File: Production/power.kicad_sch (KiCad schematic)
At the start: 4 parts, among them U204 TPS62177DQCR

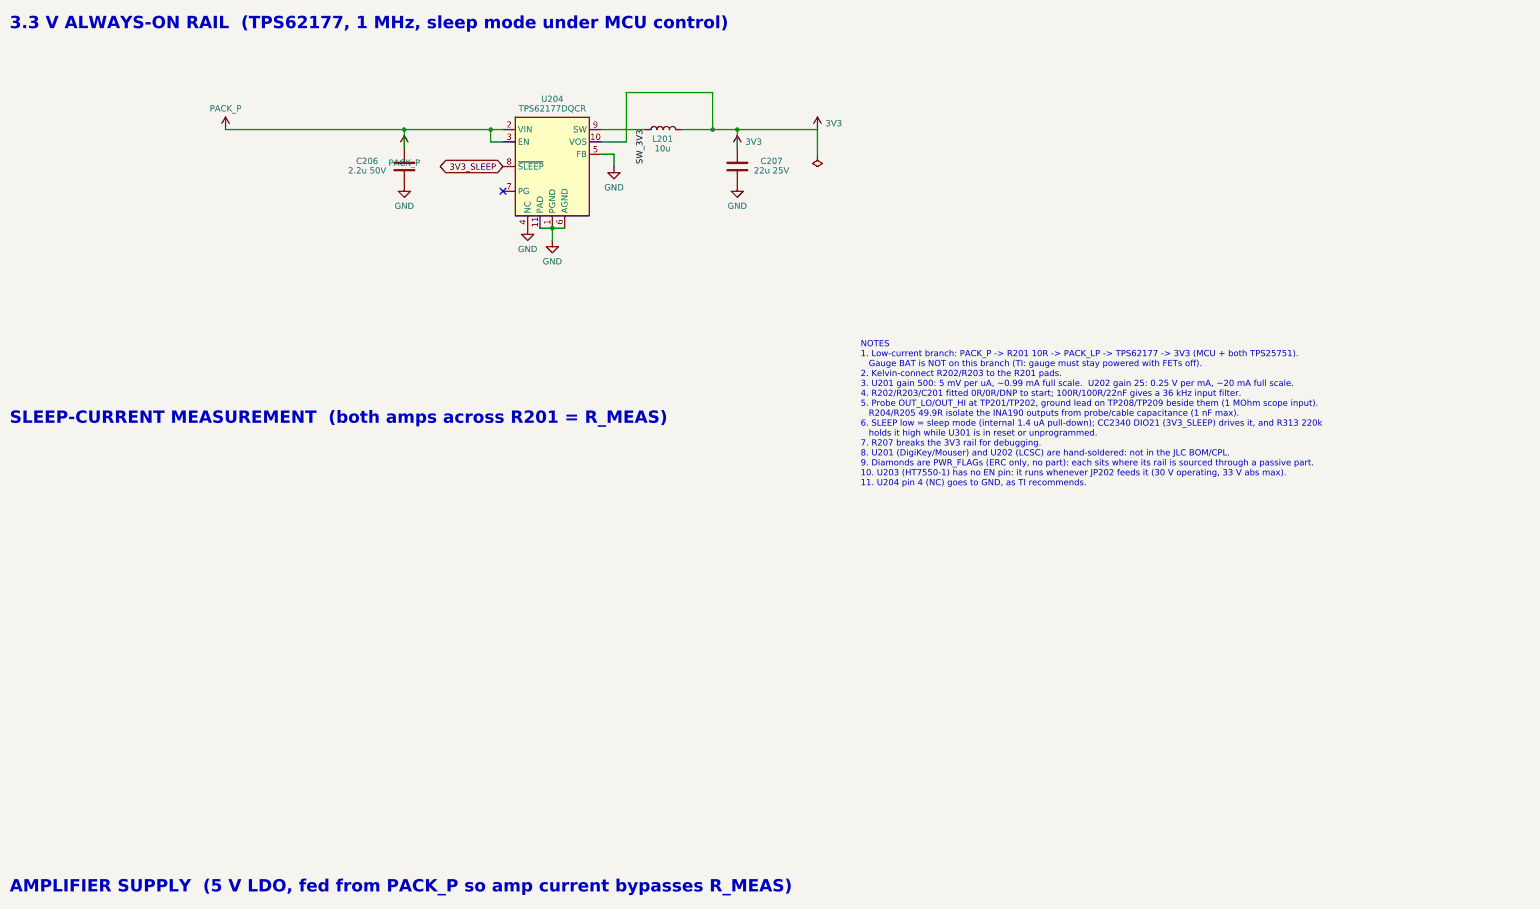
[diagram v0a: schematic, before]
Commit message: Production schematic P0: drawing tidy
tools/tidy_production.py (runs after make_production.py): pogo pads in their
own row, TC2030 under its SWD heading, link-merge leftovers removed, empty
headings deleted, sheet notes, root index and revision log rewritten for
production, sheets renamed 3V3 Rail and MCU. Netlist unchanged (check_netlist
passes); ERC: no errors.

Co-Authored-By: Claude Opus 5.5 <noreply@anthropic.com>
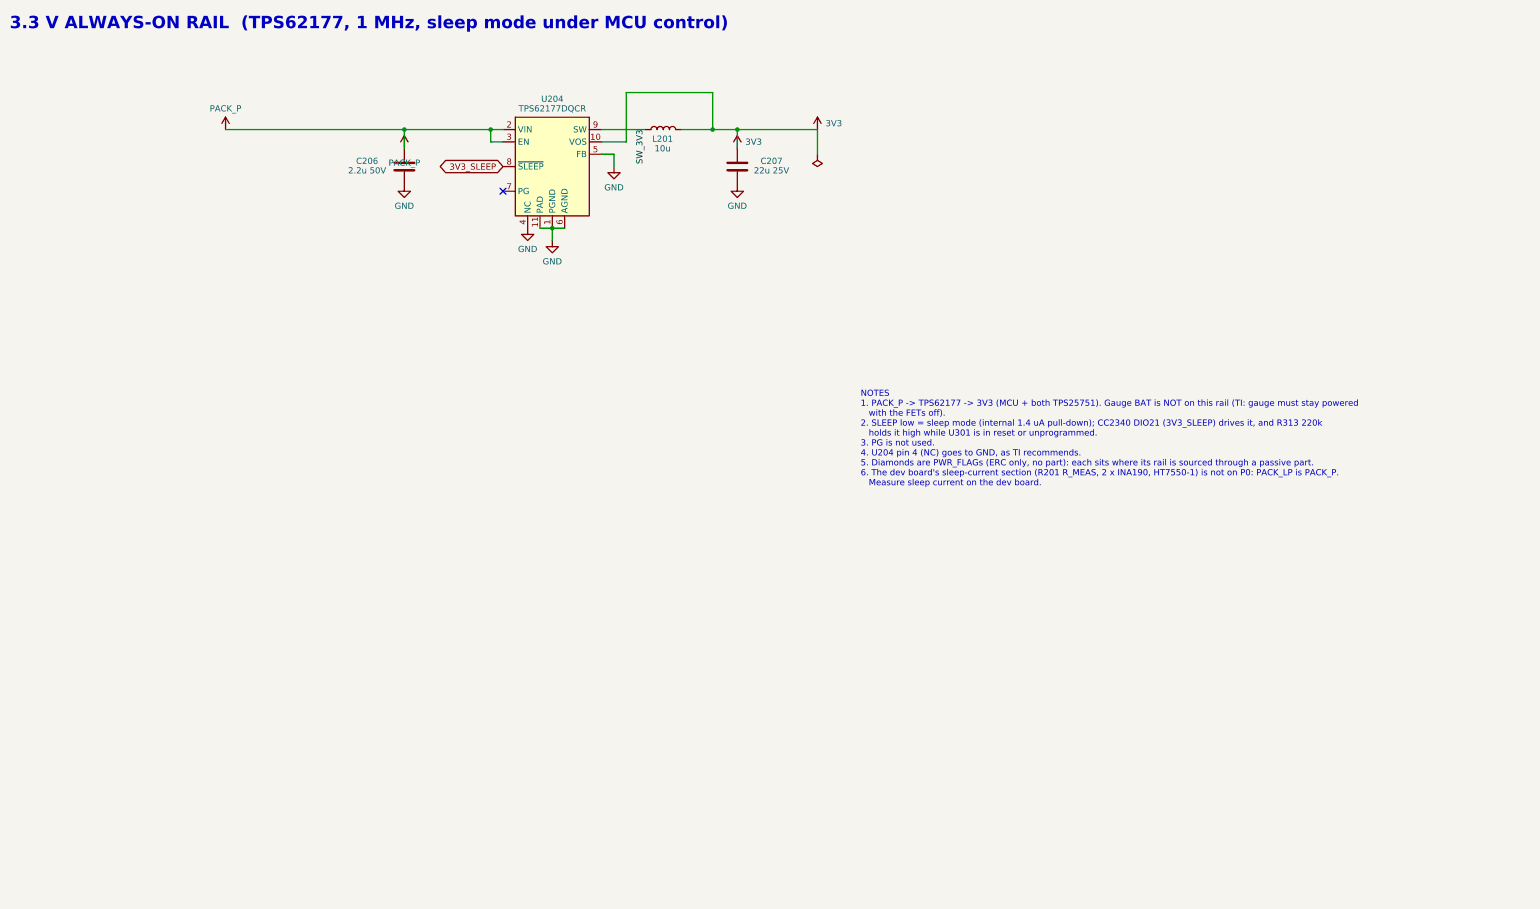
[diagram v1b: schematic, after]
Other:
- note added: "NOTES 1. PACK_P -> TPS62177 -> 3V3 (MCU + both TPS25751). Gauge BAT is NOT on this rail (TI: gauge must stay powered with the FETs off). 2. SLEEP low = sleep mode (internal 1.4 uA pull-down); CC2340 DIO21 (3V3_SLEEP) drives it, and R313 220k holds it high while U301 is in reset or unprogrammed. 3. PG is not used. 4. U204 pin 4 (NC) goes to GND, as TI recommends. 5. Diamonds are PWR_FLAGs (ERC onl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"
- note removed: "AMPLIFIER SUPPLY (5 V LDO, fed from PACK_P so amp current bypasses R_MEAS)"
- note removed: "NOTES 1. Low-current branch: PACK_P -> R201 10R -> PACK_LP -> TPS62177 -> 3V3 (MCU + both TPS25751). Gauge BAT is NOT on this branch (TI: gauge must stay powered with FETs off). 2. Kelvin-connect R202/R203 to the R201 pads. 3. U201 gain 500: 5 mV per uA, ~0.99 mA full scale. U202 gain 25: 0.25 V per mA, ~20 mA full scale. 4. R202/R203/C201 fitted 0R/0R/DNP to start; 100R/100R/22nF gives a 36 kHz 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"
- note removed: "SLEEP-CURRENT MEASUREMENT (both amps across R201 = R_MEAS)"
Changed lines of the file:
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@@
 		(rev "P0")
 		(company "Monolith 100 W battery bank - production")
-		(comment 1 "R_MEAS + INA190 x2, HT7550-1, TPS62177")
-		(comment 2 "Spec + open items: DevBoard/README.md")
+		(comment 1 "TPS62177 3V3 always-on rail")
+		(comment 2 "Spec + open items: Production/README.md")
 		(comment 3 "P0: dev board rev A8 stripped by Production/tools/make_production.py; not reviewed")
-	)
-	(text "AMPLIFIER SUPPLY  (5 V LDO, fed from PACK_P so amp current bypasses R_MEAS)"
-		(exclude_from_sim no)
-		(at 40.64 213.36 0)
-		(effects
-			(font
-				(size 2.54 2.54)
-				(bold yes)
-			)
-			(justify left bottom)
-		)
-	)
-	(text "SLEEP-CURRENT MEASUREMENT  (both amps across R201 = R_MEAS)"
-		(exclude_from_sim no)
-		(at 40.64 116.84 0)
-		(effects
-			(font
-				(size 2.54 2.54)
-				(bold yes)
-			)
-			(justify left bottom)
-		)
 	)
 	(text "3.3 V ALWAYS-ON RAIL  (TPS62177, 1 MHz, sleep mode under MCU control)"
@@
 		)
 	)
-	(text "NOTES\n1. Low-current branch: PACK_P -> R201 10R -> PACK_LP -> TPS62177 -> 3V3 (MCU + both TPS25751).\n   Gauge BAT is NOT on this branch (TI: gauge must stay powered with FETs off).\n2. Kelvin-connect R202/R203 to the R201 pads.\n3. U201 gain 500: 5 mV per uA, ~0.99 mA full scale.  U202 gain 25: 0.25 V per mA, ~20 mA full scale.\n4. R202/R203/C201 fitted 0R/0R/DNP to start; 100R/100R/22nF gives a 36 kHz input filter.\n5. Probe OUT_LO/OUT_HI at TP201/TP202, ground lead on TP208/TP209 beside them (1 MOhm scope input).\n   R204/R205 49.9R isolate the INA190 outputs from probe/cable capacitance (1 nF max).\n6. SLEEP low = sleep mode (internal 1.4 uA pull-down); CC2340 DIO21 (3V3_SLEEP) drives it, and R313 220k\n   holds it high while U301 is in reset or unprogrammed.\n7. R207 breaks the 3V3 rail for debugging.\n8. U201 (DigiKey/Mouser) and U202 (LCSC) are hand-soldered: not in the JLC BOM/CPL.\n9. Diamonds are PWR_FLAGs (ERC only, no part): each sits where its rail is sourced through a passive part.\n10. U203 (HT7550-1) has no EN pin: it runs whenever JP202 feeds it (30 V operating, 33 V abs max).\n11. U204 pin 4 (NC) goes to GND, as TI recommends."
+	(text "NOTES\n1. PACK_P -> TPS62177 -> 3V3 (MCU + both TPS25751). Gauge BAT is NOT on this rail (TI: gauge must stay powered\n   with the FETs off).\n2. SLEEP low = sleep mode (internal 1.4 uA pull-down); CC2340 DIO21 (3V3_SLEEP) drives it, and R313 220k\n   holds it high while U301 is in reset or unprogrammed.\n3. PG is not used.\n4. U204 pin 4 (NC) goes to GND, as TI recommends.\n5. Diamonds are PWR_FLAGs (ERC only, no part): each sits where its rail is sourced through a passive part.\n6. The dev board's sleep-current section (R201 R_MEAS, 2 x INA190, HT7550-1) is not on P0: PACK_LP is PACK_P.\n   Measure sleep current on the dev board."
 		(exclude_from_sim no)
 		(at 215.9 129.54 0)
@@
 	(wire
 		(pts
-			(xy 92.71 55.88) (xy 99.06 55.88)
-		)
-		(stroke
-			(width 0)
-			(type default)
-		)
-	)
-	(wire
-		(pts
 			(xy 185.42 55.88) (xy 190.5 55.88)
-		)
-		(stroke
-			(width 0)
-			(type default)
-		)
-	)
-	(wire
-		(pts
-			(xy 190.5 55.88) (xy 199.39 55.88)
-		)
-		(stroke
-			(width 0)
-			(type default)
-		)
-	)
-	(wire
-		(pts
-			(xy 106.68 55.88) (xy 121.92 55.88)
-		)
-		(stroke
-			(width 0)
-			(type default)
-		)
-	)
-	(wire
-		(pts
-			(xy 99.06 55.88) (xy 106.68 55.88)
 		)
 		(stroke
@@
 		)
 	)
-	(wire
-		(pts
-			(xy 85.09 55.88) (xy 92.71 55.88)
-		)
-		(stroke
-			(width 0)
-			(type default)
-		)
-	)
-	(wire
-		(pts
-			(xy 199.39 55.88) (xy 207.01 55.88)
-		)
-		(stroke
-			(width 0)
-			(type default)
-		)
-	)
 	(symbol
 		(lib_id "power:+3V3")
@@
 		(in_pos_files yes)
 		(dnp no)
-		(property "Reference" "#PWR9007"
+		(property "Reference" "#PWR9009"
 			(at 190.5 59.69 0)
 			(hide yes)
@@
 			(project "Monolith"
 				(path "/f83241ae-2bb3-4ed7-b986-c0a03971de0a/d9806540-c841-409c-9faa-82254b30b220"
-					(reference "#PWR9008")
+					(reference "#PWR9010")
 					(unit 1)
 				)
@@
 		(in_pos_files yes)
 		(dnp no)
-		(property "Reference" "#PWR9009"
+		(property "Reference" "#PWR9011"
 			(at 121.92 59.69 0)
 			(hide yes)
@@
 			(project "Monolith"
 				(path "/f83241ae-2bb3-4ed7-b986-c0a03971de0a/d9806540-c841-409c-9faa-82254b30b220"
-					(reference "#PWR9010")
+					(reference "#PWR9012")
 					(unit 1)
 				)
@@
 		(at 142.24 68.58)
 	)
+	(wire
+		(pts
+			(xy 190.5 55.88) (xy 207.01 55.88)
+		)
+		(stroke
+			(width 0)
+			(type default)
+		)
+	)
+	(wire
+		(pts
+			(xy 85.09 55.88) (xy 121.92 55.88)
+		)
+		(stroke
+			(width 0)
+			(type default)
+		)
+	)
 	(sheet_instances

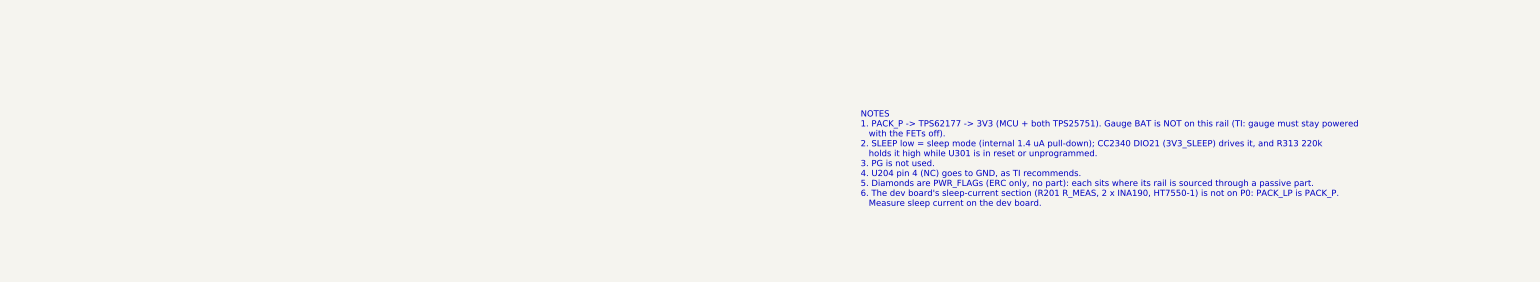
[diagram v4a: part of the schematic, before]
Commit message: Production schematic P0: direct gate drive, one shared PACK_P hybrid
R444-R447 -> copper, D406-D409 removed (gates driven directly). Battery-side
banks of both chargers, both TPS62933 inputs and the pack modelled as one bus
(tools/pack_bus_sims.py): C432/C532 hybrids -> one shared C208 on PACK_P,
C445/C545 removed. 99 uF effective (>= 80 uF C_OUT), worst part 44 %, damping
20 dB. Courtyard 2221 -> 2104 mm2. Netlist check passes; ERC clean.

Co-Authored-By: Claude Opus 5.5 <noreply@anthropic.com>
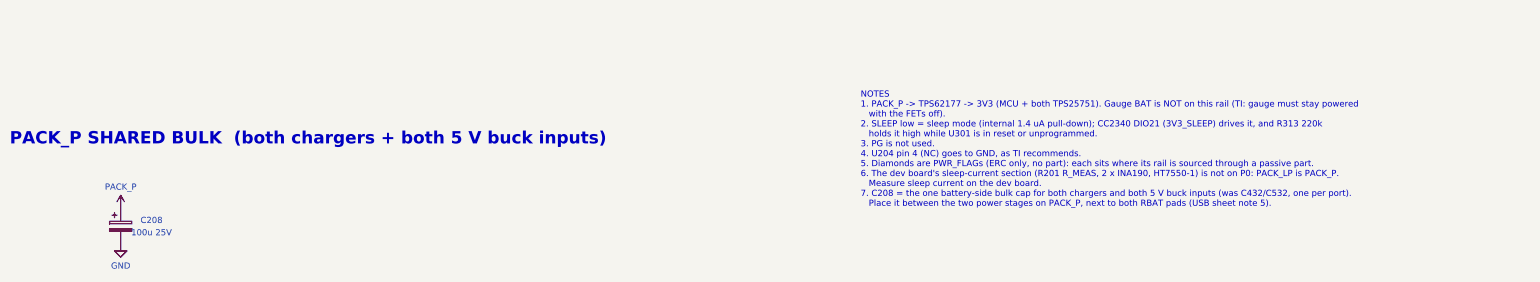
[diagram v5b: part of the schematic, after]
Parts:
- added C208: 100u 25V, Capacitor_SMD:CP_Elec_6.3x7.7, symbol Device:C_Polarized
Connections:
- net GND: now also C208.2
- net PACK_P: now also C208.1
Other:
- note added: "PACK_P SHARED BULK (both chargers + both 5 V buck inputs)"
